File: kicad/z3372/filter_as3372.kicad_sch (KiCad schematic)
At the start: 76 parts, among them Q1 MMBT3904, Q2 MMBT3904, U11 DG442xY, U18 NE5532, U19 L79L05_TO92, U4 TL074, U6 AS3360-Audio, U8 AS3372

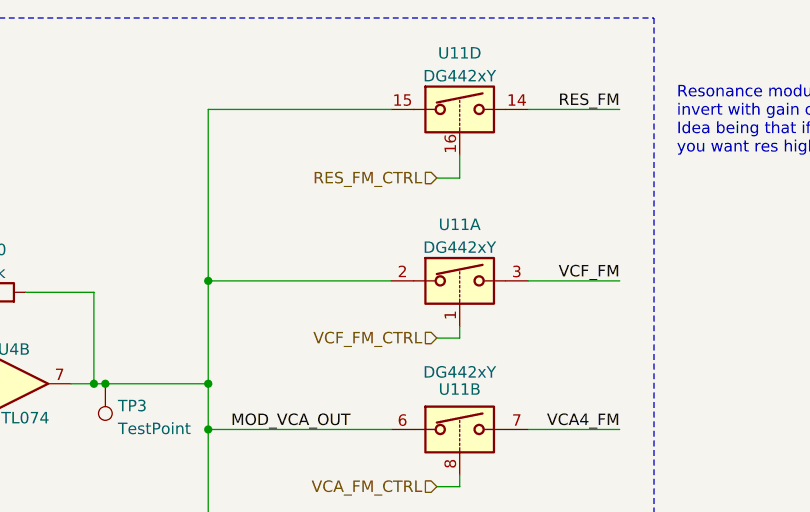
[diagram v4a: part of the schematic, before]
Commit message: unrouted = 0; still a lot of cleanup todo
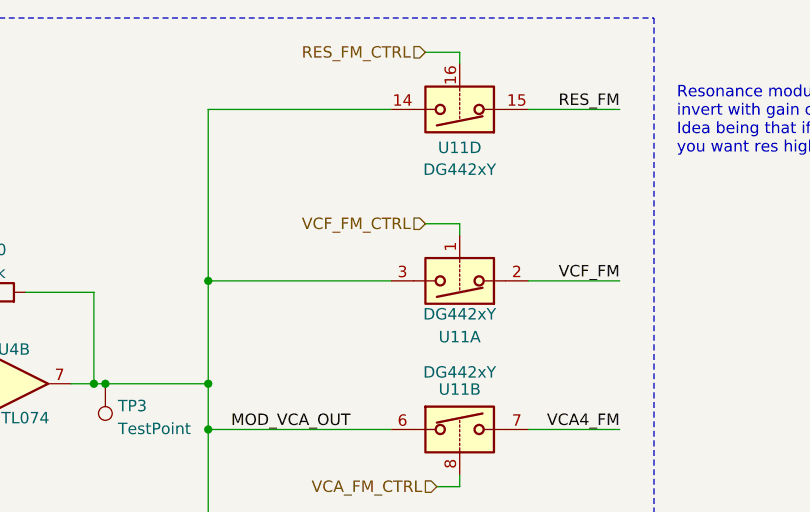
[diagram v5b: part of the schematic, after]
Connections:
- net MOD_VCA_OUT: now also U11.14, U11.3; no longer U11.15, U11.2
- net RES_FM: now also U11.15; no longer U11.14
- net VCF_FM: now also U11.2; no longer U11.3
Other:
- moved on the sheet: U11A, U11D
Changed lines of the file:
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@@
     (stroke (width 0) (type dash))
   )
-  (wire (pts (xy 193.04 48.26) (xy 195.58 48.26))
-    (stroke (width 0) (type default))
-  )
   (wire (pts (xy 146.05 128.27) (xy 146.05 130.81))
     (stroke (width 0) (type default))
@@
     (stroke (width 0) (type default))
   )
-  (wire (pts (xy 87.63 153.67) (xy 99.06 153.67))
+  (wire (pts (xy 191.77 35.56) (xy 195.58 35.56))
     (stroke (width 0) (type default))
   )
-  (wire (pts (xy 195.58 30.48) (xy 195.58 27.94))
+  (wire (pts (xy 87.63 153.67) (xy 99.06 153.67))
     (stroke (width 0) (type default))
   )
@@
     (stroke (width 0) (type default))
   )
-  (wire (pts (xy 195.58 48.26) (xy 195.58 46.99))
-    (stroke (width 0) (type default))
-  )
   (wire (pts (xy 135.89 143.51) (xy 133.35 143.51))
     (stroke (width 0) (type default))
@@
     (stroke (width 0) (type default))
   )
+  (wire (pts (xy 195.58 16.51) (xy 195.58 17.78))
+    (stroke (width 0) (type default))
+  )
   (wire (pts (xy 129.54 143.51) (xy 133.35 143.51))
     (stroke (width 0) (type default))
@@
     (stroke (width 0) (type default))
   )
+  (wire (pts (xy 191.77 16.51) (xy 195.58 16.51))
+    (stroke (width 0) (type default))
+  )
   (wire (pts (xy 133.35 144.78) (xy 133.35 143.51))
     (stroke (width 0) (type default))
@@
     (stroke (width 0) (type default))
   )
+  (wire (pts (xy 195.58 35.56) (xy 195.58 36.83))
+    (stroke (width 0) (type default))
+  )
   (wire (pts (xy 246.38 139.7) (xy 245.11 139.7))
     (stroke (width 0) (type default))
@@
     (stroke (width 0) (type default))
   )
-  (wire (pts (xy 193.04 30.48) (xy 195.58 30.48))
-    (stroke (width 0) (type default))
-  )
   (wire (pts (xy 198.12 248.92) (xy 198.12 251.46))
     (stroke (width 0) (type default))
@@
     (effects (font (size 1.27 1.27)) (justify right))
   )
-  (hierarchical_label "RES_FM_CTRL" (shape input) (at 193.04 30.48 180) (fields_autoplaced)
+  (hierarchical_label "RES_FM_CTRL" (shape input) (at 191.77 16.51 180) (fields_autoplaced)
     (effects (font (size 1.27 1.27)) (justify right))
   )
@@
     (effects (font (size 1.27 1.27)) (justify right))
   )
-  (hierarchical_label "VCF_FM_CTRL" (shape input) (at 193.04 48.26 180) (fields_autoplaced)
+  (hierarchical_label "VCF_FM_CTRL" (shape input) (at 191.77 35.56 180) (fields_autoplaced)
     (effects (font (size 1.27 1.27)) (justify right))
   )
@@
     )
   )
-  (symbol (lib_id "Analog_Switch:DG442xY") (at 195.58 22.86 0) (unit 4)
+  (symbol (lib_id "Analog_Switch:DG442xY") (at 195.58 22.86 180) (unit 4)
     (in_bom yes) (on_board yes) (dnp no) (fields_autoplaced)
-    (property "Reference" "U11" (at 195.58 16.6202 0)
+    (property "Reference" "U11" (at 195.58 27.1201 0)
       (effects (font (size 1.27 1.27)))
     )
-    (property "Value" "DG442xY" (at 195.58 19.1571 0)
+    (property "Value" "DG442xY" (at 195.58 29.5443 0)
       (effects (font (size 1.27 1.27)))
     )
-    (property "Footprint" "Package_SO:SOIC-16_3.9x9.9mm_P1.27mm" (at 195.58 25.4 0)
+    (property "Footprint" "Package_SO:SOIC-16_3.9x9.9mm_P1.27mm" (at 195.58 20.32 0)
       (effects (font (size 1.27 1.27)) hide)
     )
@@
     )
   )
-  (symbol (lib_id "Analog_Switch:DG442xY") (at 195.58 41.91 0) (unit 1)
+  (symbol (lib_id "Analog_Switch:DG442xY") (at 195.58 41.91 180) (unit 1)
     (in_bom yes) (on_board yes) (dnp no)
-    (property "Reference" "U11" (at 195.58 35.6702 0)
+    (property "Reference" "U11" (at 195.58 48.1498 0)
       (effects (font (size 1.27 1.27)))
     )
-    (property "Value" "DG442xY" (at 195.58 38.2071 0)
+    (property "Value" "DG442xY" (at 195.58 45.6129 0)
       (effects (font (size 1.27 1.27)))
     )
-    (property "Footprint" "Package_SO:SOIC-16_3.9x9.9mm_P1.27mm" (at 195.58 44.45 0)
+    (property "Footprint" "Package_SO:SOIC-16_3.9x9.9mm_P1.27mm" (at 195.58 39.37 0)
       (effects (font (size 1.27 1.27)) hide)
     )

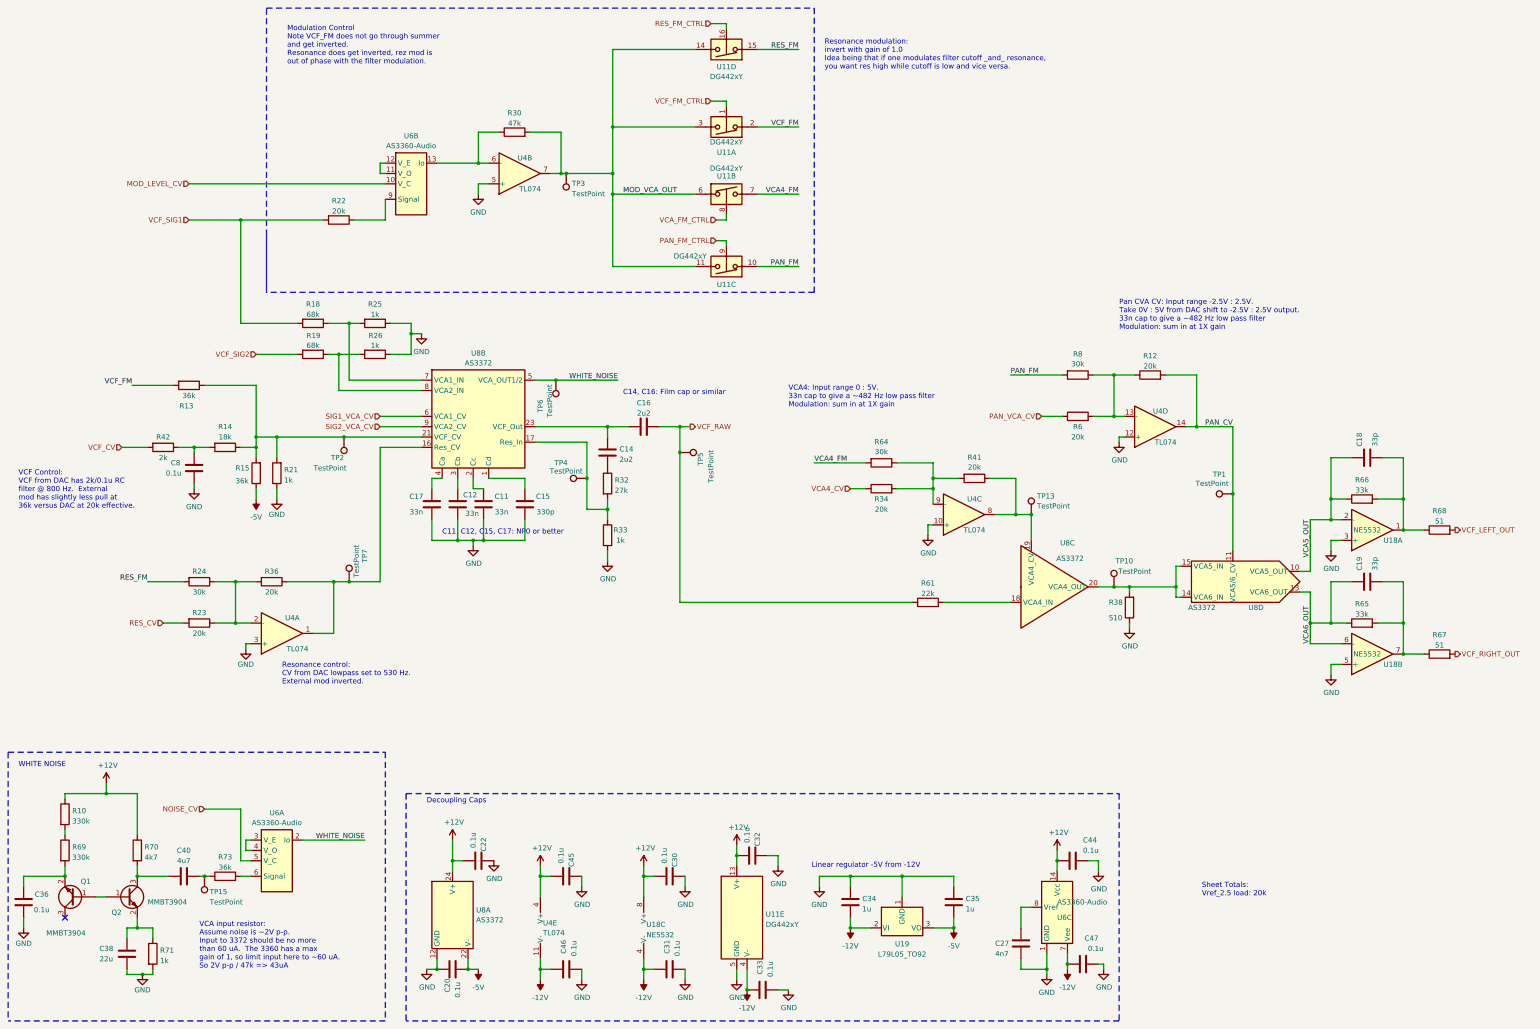
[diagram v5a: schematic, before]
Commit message: geo reannotate designators
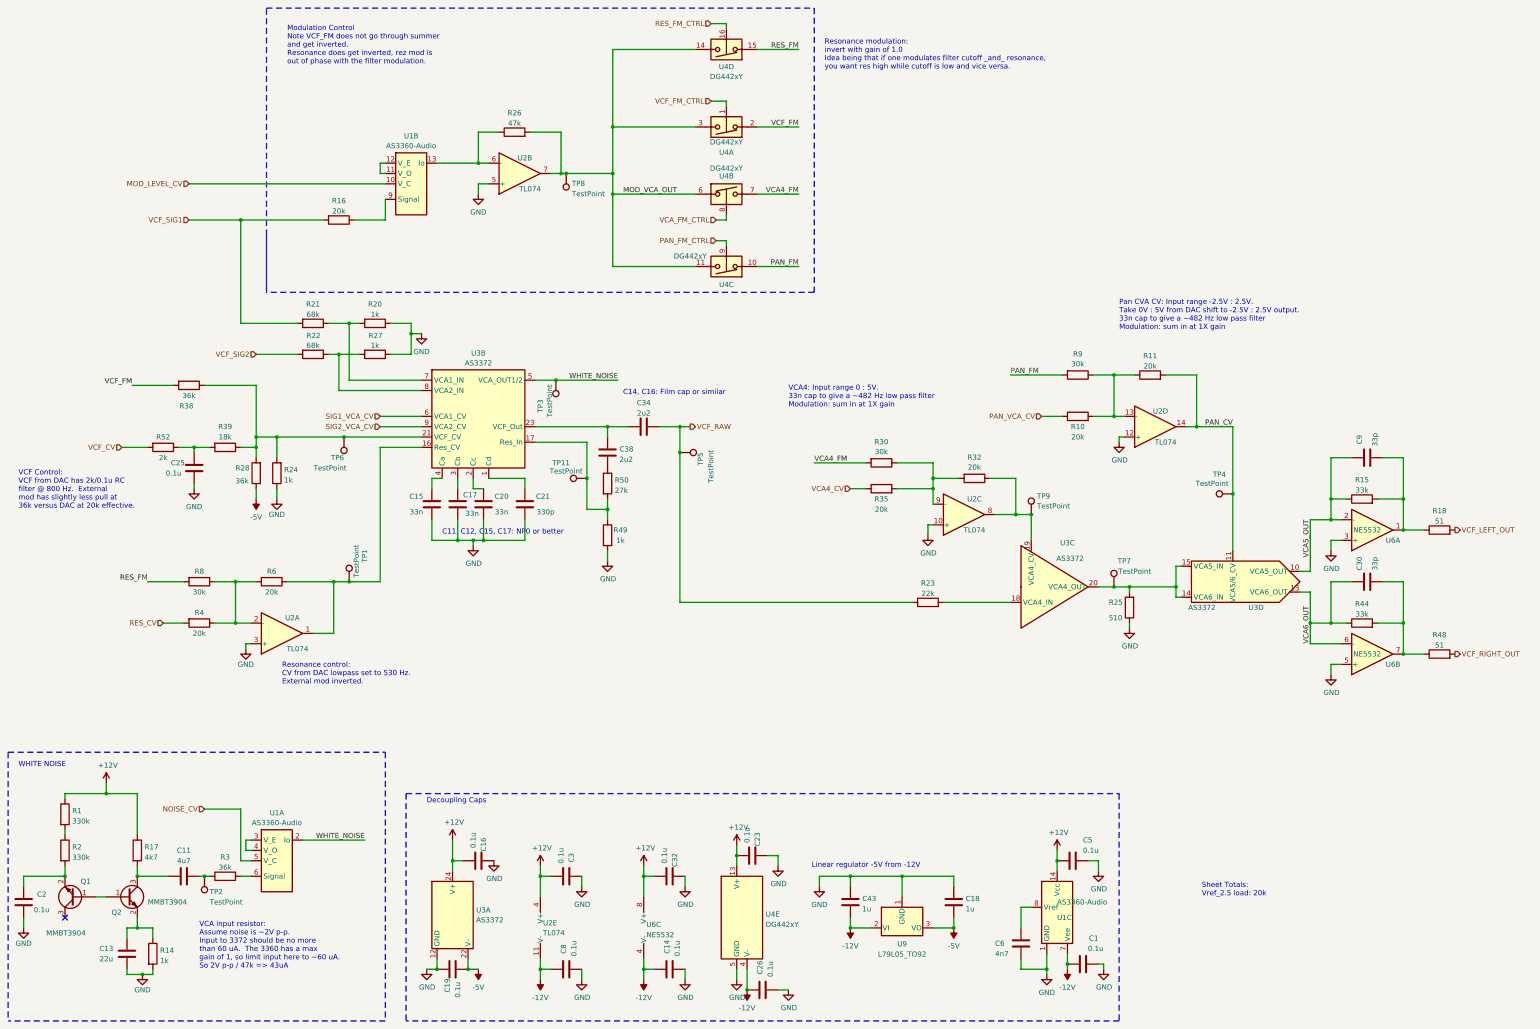
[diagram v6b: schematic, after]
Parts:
- renumbered C47 to C1, C40 to C11, C38 to C13, C31 to C14, C17 to C15, C22 to C16, C12 to C17, C35 to C18, C20 to C19, C36 to C2, C11 to C20, C15 to C21, C32 to C23, C8 to C25, C33 to C26, C45 to C3, C19 to C30, C30 to C32, C16 to C34, C14 to C38, C34 to C43, C44 to C5, C27 to C6, C46 to C8, C18 to C9, R10 to R1, R6 to R10, R12 to R11, R71 to R14, R66 to R15, R22 to R16, R70 to R17, R68 to R18, R69 to R2, R25 to R20, R18 to R21, R19 to R22, R61 to R23, R21 to R24, R38 to R25, R30 to R26, R26 to R27, R15 to R28, R73 to R3, R64 to R30, R41 to R32, R34 to R35, R13 to R38, R14 to R39, R23 to R4, R65 to R44, R67 to R48, R33 to R49, R32 to R50, R42 to R52, R36 to R6, R24 to R8, R8 to R9, TP7 to TP1, TP4 to TP11, TP15 to TP2, TP6 to TP3, TP1 to TP4, TP2 to TP6, TP10 to TP7, TP3 to TP8, TP13 to TP9, U6 to U1, U4 to U2, U8 to U3, U11 to U4, U18 to U6, U19 to U9
